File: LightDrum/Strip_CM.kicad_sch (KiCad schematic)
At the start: 26 parts, among them T701 NET-TIE, T702 NET-TIE, T703 NET-TIE, T704 NET-TIE, T705 NET-TIE, T706 NET-TIE, T707 NET-TIE, T708 NET-TIE, T709 NET-TIE, T710 NET-TIE, T711 NET-TIE, T712 NET-TIE, T713 NET-TIE, T714 NET-TIE, T715 NET-TIE, T716 NET-TIE, U701 INA4181 A2, U702 INA4181 A2

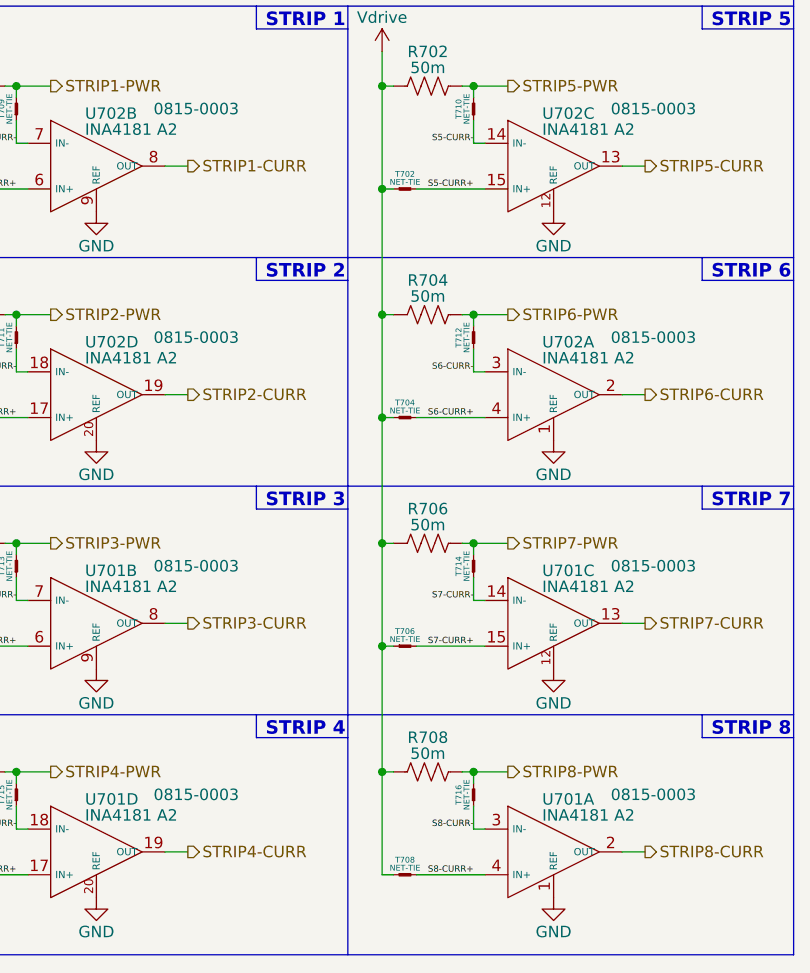
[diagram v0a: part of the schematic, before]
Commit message: Replace relays and SWD conn
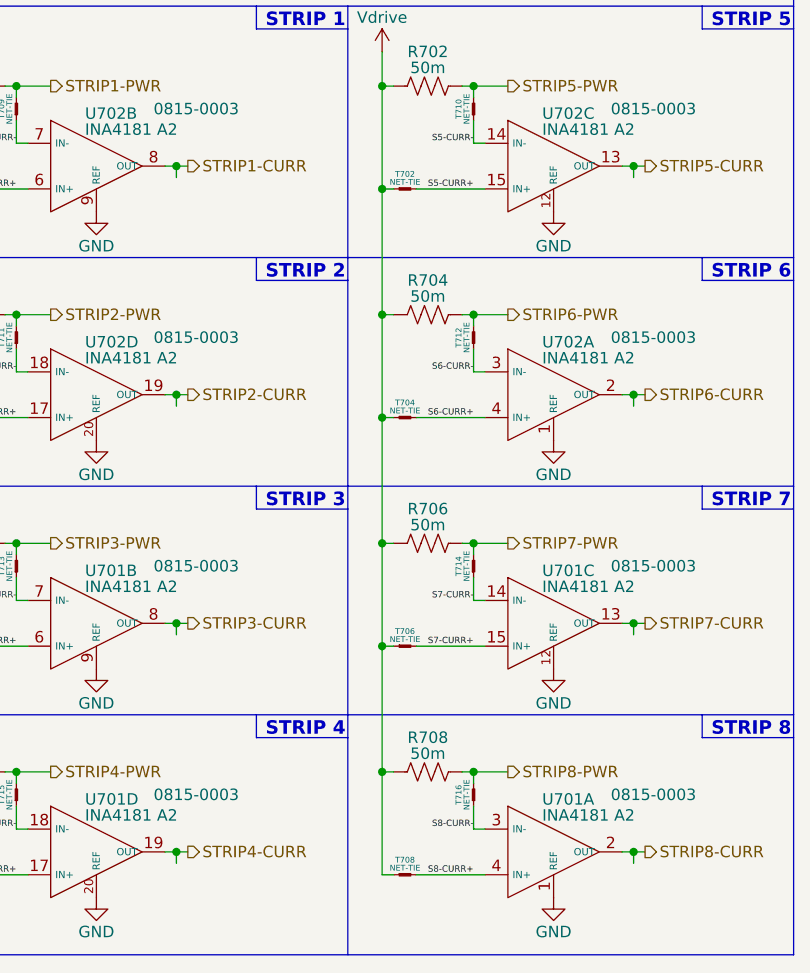
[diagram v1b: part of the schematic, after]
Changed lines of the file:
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@@
   (junction (at 21.59 55.88) (diameter 0) (color 0 0 0 0)
   )
+  (junction (at 49.53 64.77) (diameter 0) (color 0 0 0 0)
+  )
   (junction (at 72.39 92.71) (diameter 0) (color 0 0 0 0)
   )
@@
   (junction (at 72.39 81.28) (diameter 0) (color 0 0 0 0)
   )
+  (junction (at 49.53 39.37) (diameter 0) (color 0 0 0 0)
+  )
   (junction (at 82.55 55.88) (diameter 0) (color 0 0 0 0)
   )
   (junction (at 21.59 81.28) (diameter 0) (color 0 0 0 0)
   )
+  (junction (at 100.33 90.17) (diameter 0) (color 0 0 0 0)
+  )
   (junction (at 72.39 41.91) (diameter 0) (color 0 0 0 0)
   )
   (junction (at 21.59 92.71) (diameter 0) (color 0 0 0 0)
   )
+  (junction (at 100.33 39.37) (diameter 0) (color 0 0 0 0)
+  )
   (junction (at 72.39 106.68) (diameter 0) (color 0 0 0 0)
   )
+  (junction (at 49.53 115.57) (diameter 0) (color 0 0 0 0)
+  )
   (junction (at 82.55 30.48) (diameter 0) (color 0 0 0 0)
   )
+  (junction (at 100.33 64.77) (diameter 0) (color 0 0 0 0)
+  )
+  (junction (at 100.33 115.57) (diameter 0) (color 0 0 0 0)
+  )
+  (junction (at 49.53 90.17) (diameter 0) (color 0 0 0 0)
+  )
+  (wire (pts (xy 100.33 90.17) (xy 100.33 91.44))
+    (stroke (width 0) (type default))
+  )
   (wire (pts (xy 72.39 30.48) (xy 72.39 41.91))
     (stroke (width 0) (type default))
@@
     (stroke (width 0) (type default))
   )
+  (wire (pts (xy 100.33 90.17) (xy 101.6 90.17))
+    (stroke (width 0) (type default))
+  )
   (wire (pts (xy 31.75 110.49) (xy 31.75 113.03))
     (stroke (width 0) (type default))
@@
     (stroke (width 0) (type default))
   )
-  (wire (pts (xy 99.06 115.57) (xy 101.6 115.57))
+  (wire (pts (xy 99.06 115.57) (xy 100.33 115.57))
     (stroke (width 0) (type default))
   )
@@
     (stroke (width 0) (type default))
   )
-  (wire (pts (xy 99.06 39.37) (xy 101.6 39.37))
+  (wire (pts (xy 100.33 39.37) (xy 101.6 39.37))
+    (stroke (width 0) (type default))
+  )
+  (wire (pts (xy 99.06 39.37) (xy 100.33 39.37))
     (stroke (width 0) (type default))
   )
@@
     (stroke (width 0) (type default))
   )
-  (wire (pts (xy 48.26 39.37) (xy 50.8 39.37))
+  (wire (pts (xy 48.26 39.37) (xy 49.53 39.37))
     (stroke (width 0) (type default))
   )
@@
     (stroke (width 0) (type default))
   )
-  (wire (pts (xy 48.26 64.77) (xy 50.8 64.77))
+  (wire (pts (xy 48.26 64.77) (xy 49.53 64.77))
     (stroke (width 0) (type default))
   )
@@
     (stroke (width 0) (type default))
   )
+  (wire (pts (xy 100.33 39.37) (xy 100.33 40.64))
+    (stroke (width 0) (type default))
+  )
   (wire (pts (xy 31.75 30.48) (xy 31.75 31.75))
     (stroke (width 0) (type default))
@@
     (stroke (width 0) (type default))
   )
+  (wire (pts (xy 49.53 115.57) (xy 50.8 115.57))
+    (stroke (width 0) (type default))
+  )
   (polyline (pts (xy 16.51 16.51) (xy 118.11 16.51))
     (stroke (width 0) (type default))
@@
     (stroke (width 0) (type default))
   )
+  (wire (pts (xy 49.53 64.77) (xy 49.53 66.04))
+    (stroke (width 0) (type default))
+  )
   (wire (pts (xy 82.55 110.49) (xy 82.55 113.03))
     (stroke (width 0) (type default))
@@
     (stroke (width 0) (type default))
   )
-  (wire (pts (xy 48.26 90.17) (xy 50.8 90.17))
+  (wire (pts (xy 48.26 90.17) (xy 49.53 90.17))
+    (stroke (width 0) (type default))
+  )
+  (wire (pts (xy 100.33 64.77) (xy 100.33 66.04))
+    (stroke (width 0) (type default))
+  )
+  (wire (pts (xy 49.53 90.17) (xy 49.53 91.44))
     (stroke (width 0) (type default))
   )
@@
     (stroke (width 0) (type default))
   )
+  (wire (pts (xy 49.53 39.37) (xy 49.53 40.64))
+    (stroke (width 0) (type default))
+  )
   (wire (pts (xy 82.55 55.88) (xy 86.36 55.88))
     (stroke (width 0) (type default))
@@
     (stroke (width 0) (type default))
   )
+  (wire (pts (xy 100.33 115.57) (xy 100.33 116.84))
+    (stroke (width 0) (type default))
+  )
   (wire (pts (xy 72.39 55.88) (xy 72.39 67.31))
     (stroke (width 0) (type default))
@@
     (stroke (width 0) (type default))
   )
-  (wire (pts (xy 99.06 64.77) (xy 101.6 64.77))
+  (wire (pts (xy 99.06 64.77) (xy 100.33 64.77))
     (stroke (width 0) (type default))
   )
@@
     (stroke (width 0) (type default))
   )
+  (wire (pts (xy 49.53 90.17) (xy 50.8 90.17))
+    (stroke (width 0) (type default))
+  )
   (wire (pts (xy 21.59 67.31) (xy 21.59 81.28))
     (stroke (width 0) (type default))
   )
+  (wire (pts (xy 49.53 39.37) (xy 50.8 39.37))
+    (stroke (width 0) (type default))
+  )
   (wire (pts (xy 21.59 41.91) (xy 21.59 55.88))
     (stroke (width 0) (type default))
@@
     (stroke (width 0) (type default))
   )
-  (wire (pts (xy 99.06 90.17) (xy 101.6 90.17))
+  (wire (pts (xy 99.06 90.17) (xy 100.33 90.17))
+    (stroke (width 0) (type default))
+  )
+  (wire (pts (xy 100.33 64.77) (xy 101.6 64.77))
+    (stroke (width 0) (type default))
+  )
+  (wire (pts (xy 49.53 64.77) (xy 50.8 64.77))
     (stroke (width 0) (type default))
   )
@@
     (stroke (width 0) (type default))
   )
+  (wire (pts (xy 49.53 115.57) (xy 49.53 116.84))
+    (stroke (width 0) (type default))
+  )
   (polyline (pts (xy 118.11 52.07) (xy 107.95 52.07))
     (stroke (width 0) (type default))
@@
     (stroke (width 0) (type default))
   )
+  (wire (pts (xy 100.33 115.57) (xy 101.6 115.57))
+    (stroke (width 0) (type default))
+  )
   (wire (pts (xy 31.75 106.68) (xy 35.56 106.68))
     (stroke (width 0) (type default))
@@
     (stroke (width 0) (type default))
   )
-  (wire (pts (xy 48.26 115.57) (xy 50.8 115.57))
+  (wire (pts (xy 48.26 115.57) (xy 49.53 115.57))
     (stroke (width 0) (type default))
   )
@@
     (effects (font (size 1.27 1.27)) (justify left))
   )
+  (netclass_flag "" (length 2.54) (shape round) (at 100.33 116.84 180) (fields_autoplaced)
+    (effects (font (size 1.27 1.27)) (justify right bottom))
+    (property "Netclass" "ALG-SIG" (at 101.0285 119.38 0)
+      (effects (font (size 1.27 1.27) italic) (justify left))
+    )
+  )
+  (netclass_flag "" (length 2.54) (shape round) (at 49.53 40.64 180) (fields_autoplaced)
+    (effects (font (size 1.27 1.27)) (justify right bottom))
+    (property "Netclass" "ALG-SIG" (at 50.2285 43.18 0)
+      (effects (font (size 1.27 1.27) italic) (justify left))
+    )
+  )
+  (netclass_flag "" (length 2.54) (shape round) (at 100.33 66.04 180) (fields_autoplaced)
+    (effects (font (size 1.27 1.27)) (justify right bottom))
+    (property "Netclass" "ALG-SIG" (at 101.0285 68.58 0)
+      (effects (font (size 1.27 1.27) italic) (justify left))
+    )
+  )
+  (netclass_flag "" (length 2.54) (shape round) (at 49.53 116.84 180) (fields_autoplaced)
+    (effects (font (size 1.27 1.27)) (justify right bottom))
+    (property "Netclass" "ALG-SIG" (at 50.2285 119.38 0)
+      (effects (font (size 1.27 1.27) italic) (justify left))
+    )
+  )
+  (netclass_flag "" (length 2.54) (shape round) (at 49.53 91.44 180) (fields_autoplaced)
+    (effects (font (size 1.27 1.27)) (justify right bottom))
+    (property "Netclass" "ALG-SIG" (at 50.2285 93.98 0)
+      (effects (font (size 1.27 1.27) italic) (justify left))
+    )
+  )
+  (netclass_flag "" (length 2.54) (shape round) (at 49.53 66.04 180) (fields_autoplaced)
+    (effects (font (size 1.27 1.27)) (justify right bottom))
+    (property "Netclass" "ALG-SIG" (at 50.2285 68.58 0)
+      (effects (font (size 1.27 1.27) italic) (justify left))
+    )
+  )
+  (netclass_flag "" (length 2.54) (shape round) (at 100.33 40.64 180) (fields_autoplaced)
+    (effects (font (size 1.27 1.27)) (justify right bottom))
+    (property "Netclass" "ALG-SIG" (at 101.0285 43.18 0)
+      (effects (font (size 1.27 1.27) italic) (justify left))
+    )
+  )
+  (netclass_flag "" (length 2.54) (shape round) (at 100.33 91.44 180) (fields_autoplaced)
+    (effects (font (size 1.27 1.27)) (justify right bottom))
+    (property "Netclass" "ALG-SIG" (at 101.0285 93.98 0)
+      (effects (font (size 1.27 1.27) italic) (justify left))
+    )
+  )
   (symbol (lib_id "Daxxn_IC:INA4181") (at 90.17 115.57 0) (unit 1)

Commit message: Preliminary schematic lock - Starting PCB layout
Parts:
- R701, R702, R703, R704, R705, R706, R707, R708: SupplierPN (none) -> 541-10110-1-ND
- U701, U702: SupplierPN (none) -> 296-49082-1-ND
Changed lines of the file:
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@@
   (title_block
     (title "LightDrum")
-    (rev "REV10")
+    (rev "REV11")
     (company "Daxxn Industries")
   )
@@
     (property "PartNumber" "0815-0003" (at 97.79 109.22 0)
       (effects (font (size 1.27 1.27)) (justify left))
+    )
+    (property "SupplierPN" "296-49082-1-ND" (at 90.17 115.57 0)
+      (effects (font (size 1.27 1.27)) hide)
     )
     (pin "10")
@@
       (effects (font (size 1.27 1.27)) hide)
     )
+    (property "SupplierPN" "~" (at 82.55 33.02 0)
+      (effects (font (size 1.27 1.27)) hide)
+    )
     (pin "1")
     (pin "2")
@@
       (effects (font (size 1.27 1.27)) hide)
     )
+    (property "SupplierPN" "~" (at 24.13 92.71 0)
+      (effects (font (size 1.27 1.27)) hide)
+    )
     (pin "1")
     (pin "2")
@@
       (effects (font (size 1.27 1.27)) hide)
     )
+    (property "SupplierPN" "541-10110-1-ND" (at 77.47 106.68 0)
+      (effects (font (size 1.27 1.27)) hide)
+    )
     (pin "1")
     (pin "2")
@@
       (effects (font (size 1.27 1.27)) hide)
     )
+    (property "SupplierPN" "~" (at 74.93 41.91 0)
+      (effects (font (size 1.27 1.27)) hide)
+    )
     (pin "1")
     (pin "2")
@@
       (effects (font (size 1.27 1.27)) hide)
     )
+    (property "SupplierPN" "541-10110-1-ND" (at 77.47 81.28 0)
+      (effects (font (size 1.27 1.27)) hide)
+    )
     (pin "1")
     (pin "2")
@@
       (effects (font (size 1.27 1.27)) hide)
     )
+    (property "SupplierPN" "~" (at 31.75 83.82 0)
+      (effects (font (size 1.27 1.27)) hide)
+    )
     (pin "1")
     (pin "2")
@@
     (property "PartNumber" "0815-0003" (at 46.99 33.02 0)
       (effects (font (size 1.27 1.27)) (justify left))
+    )
+    (property "SupplierPN" "296-49082-1-ND" (at 39.37 39.37 0)
+      (effects (font (size 1.27 1.27)) hide)
     )
     (pin "10")
@@
       (effects (font (size 1.27 1.27)) (justify left))
     )
+    (property "SupplierPN" "296-49082-1-ND" (at 39.37 115.57 0)
+      (effects (font (size 1.27 1.27)) hide)
+    )
     (pin "10")
     (pin "11")
@@
       (effects (font (size 1.27 1.27)) hide)
     )
+    (property "SupplierPN" "541-10110-1-ND" (at 26.67 81.28 0)
+      (effects (font (size 1.27 1.27)) hide)
+    )
     (pin "1")
     (pin "2")
@@
       (effects (font (size 1.27 1.27)) hide)
     )
+    (property "SupplierPN" "~" (at 24.13 41.91 0)
+      (effects (font (size 1.27 1.27)) hide)
+    )
     (pin "1")
     (pin "2")
@@
       (effects (font (size 1.27 1.27)) hide)
     )
+    (property "SupplierPN" "~" (at 74.93 92.71 0)
+      (effects (font (size 1.27 1.27)) hide)
+    )
     (pin "1")
     (pin "2")
@@
       (effects (font (size 1.27 1.27)) hide)
     )
+    (property "SupplierPN" "~" (at 82.55 58.42 0)
+      (effects (font (size 1.27 1.27)) hide)
+    )
     (pin "1")
     (pin "2")
@@
     (property "PartNumber" "0815-0003" (at 97.79 58.42 0)
       (effects (font (size 1.27 1.27)) (justify left))
+    )
+    (property "SupplierPN" "296-49082-1-ND" (at 90.17 64.77 0)
+      (effects (font (size 1.27 1.27)) hide)
     )
     (pin "10")
@@
       (effects (font (size 1.27 1.27)) hide)
     )
+    (property "SupplierPN" "~" (at 74.93 118.11 0)
+      (effects (font (size 1.27 1.27)) hide)
+    )
     (pin "1")
     (pin "2")
@@
       (effects (font (size 1.27 1.27)) hide)
     )
+    (property "SupplierPN" "~" (at 31.75 109.22 0)
+      (effects (font (size 1.27 1.27)) hide)
+    )
     (pin "1")
     (pin "2")
@@
       (effects (font (size 1.27 1.27)) hide)
     )
+    (property "SupplierPN" "~" (at 82.55 83.82 0)
+      (effects (font (size 1.27 1.27)) hide)
+    )
     (pin "1")
     (pin "2")
@@
     (property "PartNumber" "0815-0003" (at 46.99 58.42 0)
       (effects (font (size 1.27 1.27)) (justify left))
+    )
+    (property "SupplierPN" "296-49082-1-ND" (at 39.37 64.77 0)
+      (effects (font (size 1.27 1.27)) hide)
     )
     (pin "10")
@@
       (effects (font (size 1.27 1.27)) hide)
     )
+    (property "SupplierPN" "~" (at 74.93 67.31 0)
+      (effects (font (size 1.27 1.27)) hide)
+    )
     (pin "1")
     (pin "2")
@@
       (effects (font (size 1.27 1.27)) hide)
     )
+    (property "SupplierPN" "541-10110-1-ND" (at 77.47 55.88 0)
+      (effects (font (size 1.27 1.27)) hide)
+    )
     (pin "1")
     (pin "2")
@@
     (property "PartNumber" "0815-0003" (at 97.79 83.82 0)
       (effects (font (size 1.27 1.27)) (justify left))
+    )
+    (property "SupplierPN" "296-49082-1-ND" (at 90.17 90.17 0)
+      (effects (font (size 1.27 1.27)) hide)
     )
     (pin "10")
@@
       (effects (font (size 1.27 1.27)) (justify left))
     )
+    (property "SupplierPN" "296-49082-1-ND" (at 90.17 39.37 0)
+      (effects (font (size 1.27 1.27)) hide)
+    )
     (pin "10")
     (pin "11")
@@
       (effects (font (size 1.27 1.27)) hide)
     )
+    (property "SupplierPN" "~" (at 31.75 33.02 0)
+      (effects (font (size 1.27 1.27)) hide)
+    )
     (pin "1")
     (pin "2")
@@
       (effects (font (size 1.27 1.27)) hide)
     )
+    (property "SupplierPN" "~" (at 82.55 109.22 0)
+      (effects (font (size 1.27 1.27)) hide)
+    )
     (pin "1")
     (pin "2")
@@
       (effects (font (size 1.27 1.27)) hide)
     )
+    (property "SupplierPN" "541-10110-1-ND" (at 26.67 30.48 0)
+      (effects (font (size 1.27 1.27)) hide)
+    )
     (pin "1")
     (pin "2")
@@
     (property "PartNumber" "0815-0003" (at 46.99 83.82 0)
       (effects (font (size 1.27 1.27)) (justify left))
+    )
+    (property "SupplierPN" "296-49082-1-ND" (at 39.37 90.17 0)
+      (effects (font (size 1.27 1.27)) hide)
     )
     (pin "10")
@@
       (effects (font (size 1.27 1.27)) hide)
     )
+    (property "SupplierPN" "541-10110-1-ND" (at 26.67 55.88 0)
+      (effects (font (size 1.27 1.27)) hide)
+    )
     (pin "1")
     (pin "2")
@@
       (effects (font (size 1.27 1.27)) hide)
     )
+    (property "SupplierPN" "541-10110-1-ND" (at 26.67 106.68 0)
+      (effects (font (size 1.27 1.27)) hide)
+    )
     (pin "1")
     (pin "2")
@@
       (effects (font (size 1.27 1.27)) hide)
     )
+    (property "SupplierPN" "~" (at 24.13 118.11 0)
+      (effects (font (size 1.27 1.27)) hide)
+    )
     (pin "1")
     (pin "2")
@@
       (effects (font (size 1.27 1.27)) hide)
     )
+    (property "SupplierPN" "541-10110-1-ND" (at 77.47 30.48 0)
+      (effects (font (size 1.27 1.27)) hide)
+    )
     (pin "1")
     (pin "2")
@@
       (effects (font (size 1.27 1.27)) hide)
     )
+    (property "SupplierPN" "~" (at 31.75 58.42 0)
+      (effects (font (size 1.27 1.27)) hide)
+    )
     (pin "1")
     (pin "2")
@@
       (effects (font (size 1.27 1.27)) hide)
     )
+    (property "SupplierPN" "~" (at 24.13 67.31 0)
+      (effects (font (size 1.27 1.27)) hide)
+    )
